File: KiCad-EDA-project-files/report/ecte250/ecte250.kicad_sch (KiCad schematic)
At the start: 8 parts, among them U1 LM2596S-5, U2 ADXL343

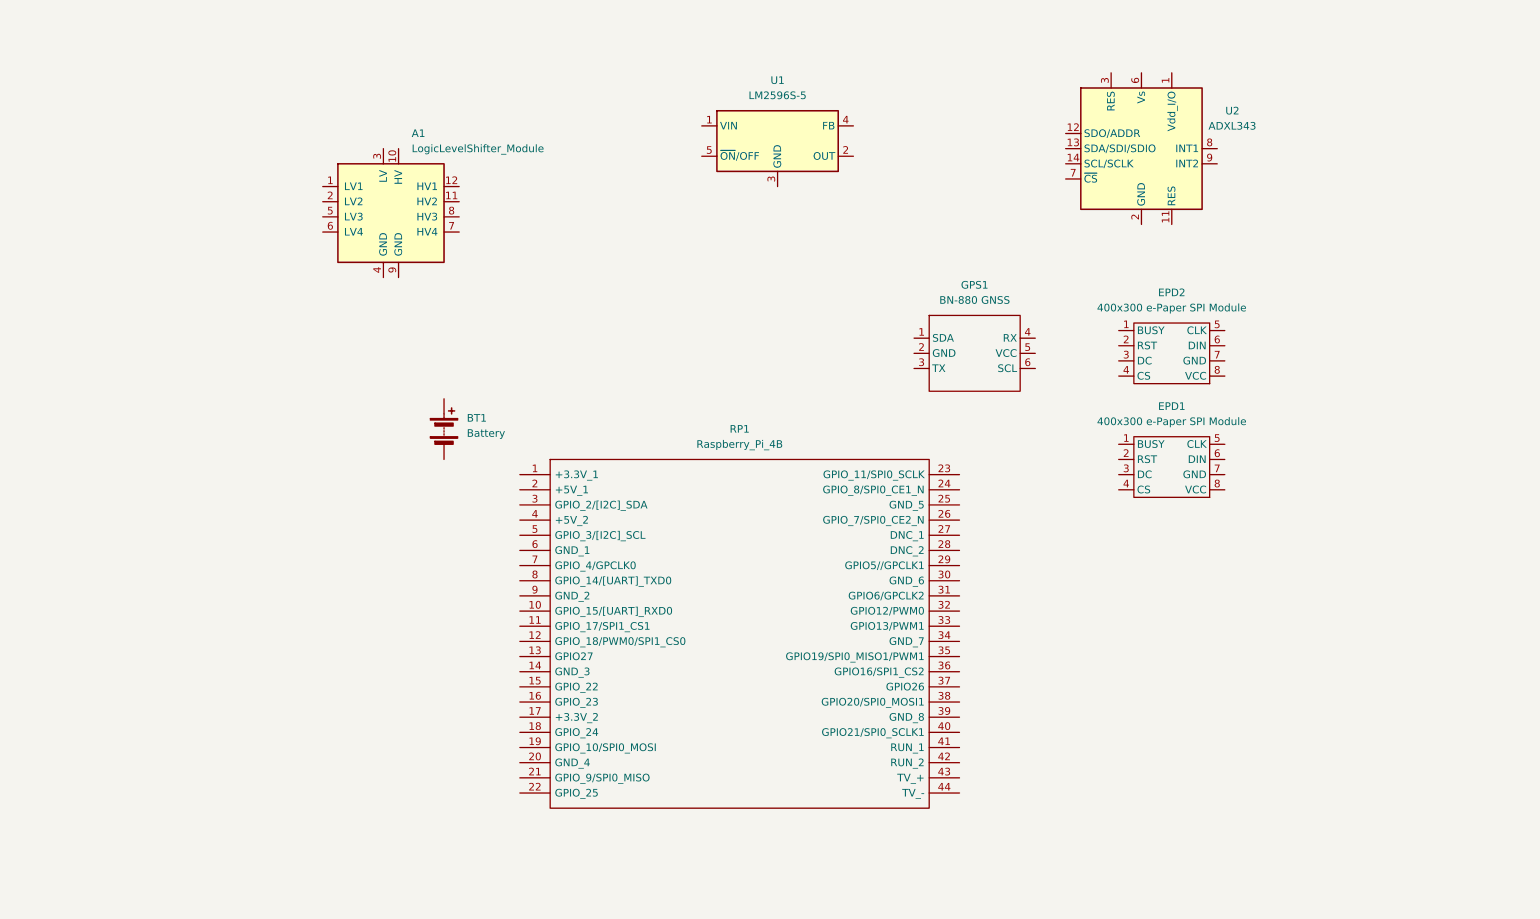
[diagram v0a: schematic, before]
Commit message: Added components used in exhibition
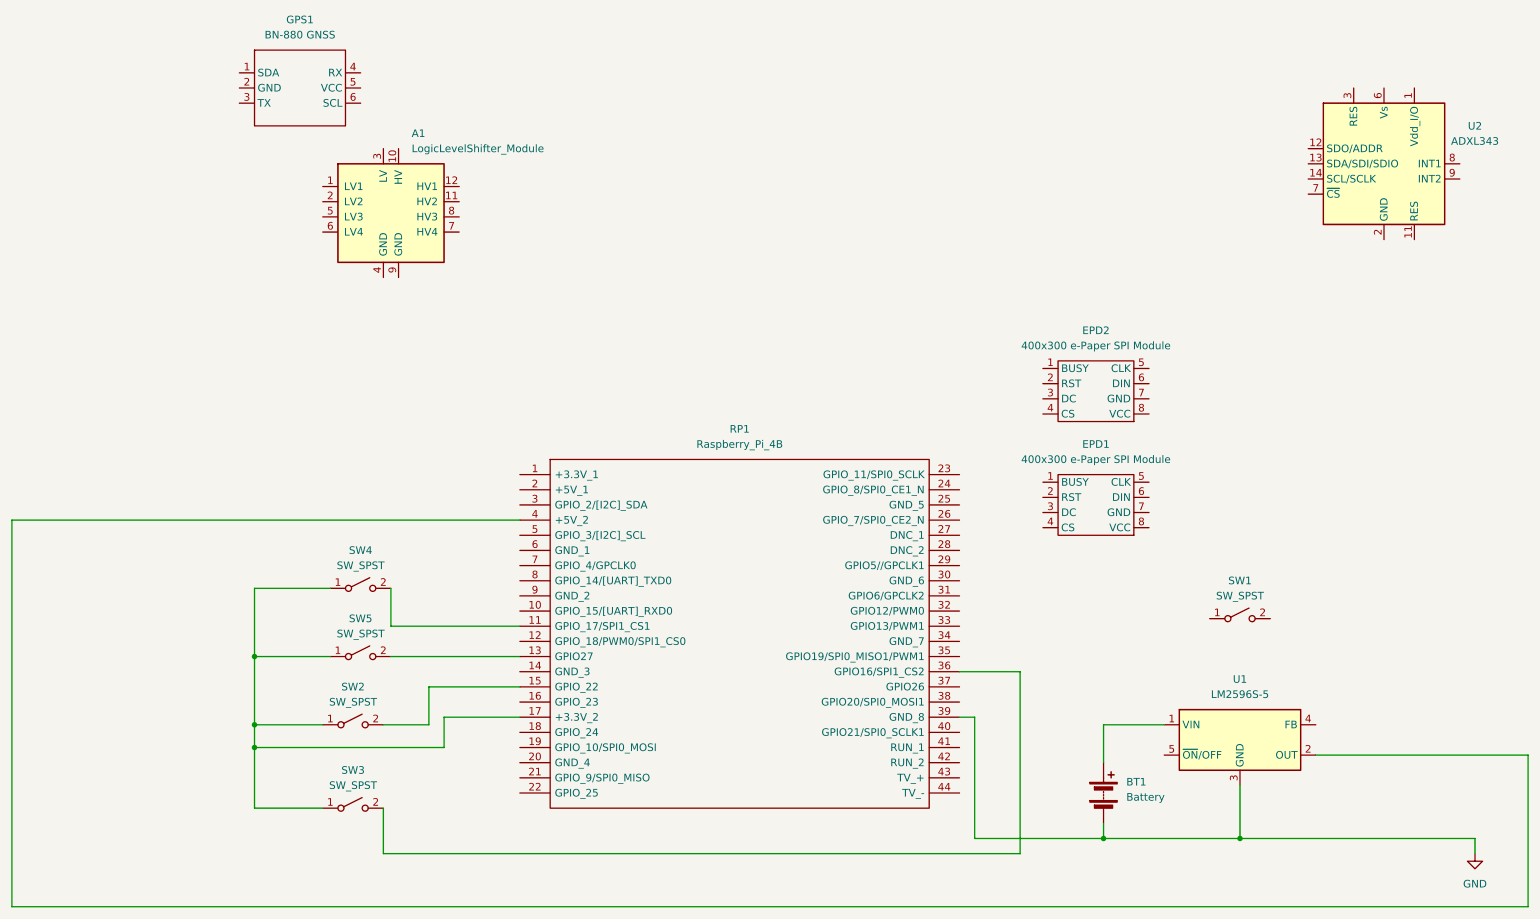
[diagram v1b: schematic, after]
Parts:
- added SW1, SW2, SW3, SW4, SW5: SW_SPST, symbol Switch:SW_SPST
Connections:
- net at U1.1 (VIN): now also BT1.1 (+)
- net at U1.2 (OUT): now also RP1.4 (+5V_2)
- net GND: now reaches U1.3 (GND)
- net GND: now also BT1.2 (-), RP1.39 (GND_8)
- net at RP1.11 (GPIO_17/SPI1_CS1): now also SW4.2 (B)
- net at RP1.13 (GPIO27): now also SW5.2 (B)
- net at RP1.15 (GPIO_22): now also SW2.2 (B)
- net at RP1.17 (+3.3V_2): now also SW2.1 (A), SW3.1 (A), SW4.1 (A), SW5.1 (A)
- net at RP1.36 (GPIO16/SPI1_CS2): now also SW3.2 (B)
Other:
- moved on the sheet: BT1, EPD1, EPD2, GPS1, U1, U2

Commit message: updated schematic files
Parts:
- BT1: value Battery -> 2s Li-Po
- U2: value ADXL343 -> ADXL345
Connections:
- net GND: now also A1.4 (GND), A1.9 (GND), EPD1.7 (GND), EPD2.7 (GND), GPS1.2 (GND), U2.2 (GND), U2.4 (GND), U2.5 (GND)
- net at U1.2 (OUT): now also SW1.1 (A); no longer RP1.4 (+5V_2)
- net at A1.1 (LV1): now also RP1.10 (GPIO_15/[UART]_RXD0)
- net at A1.10 (HV): now also GPS1.5 (VCC), RP1.2 (+5V_1)
- net at A1.11 (HV2): now also GPS1.4 (RX)
- net at A1.12 (HV1): now also GPS1.3 (TX)
- net at A1.2 (LV2): now also RP1.8 (GPIO_14/[UART]_TXD0)
- net at A1.3 (LV): now also EPD1.8 (VCC), EPD2.8 (VCC), RP1.1 (+3.3V_1), U2.6 (Vs)
- net at A1.7 (HV4): now also GPS1.1 (SDA)
- net at A1.8 (HV3): now also GPS1.6 (SCL)
- net at SW1.2 (B): now also RP1.4 (+5V_2)
- net at RP1.23 (GPIO_11/SPI0_SCLK): now also EPD1.5 (CLK), EPD2.5 (CLK)
- net at RP1.3 (GPIO_2/[I2C]_SDA): now also U2.13 (SDA/SDI/SDIO)
- net at RP1.5 (GPIO_3/[I2C]_SCL): now also U2.14 (SCL/SCLK)
- no-connect marks 0 -> 9
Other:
- moved on the sheet: A1, EPD1, GPS1, RP1, SW1

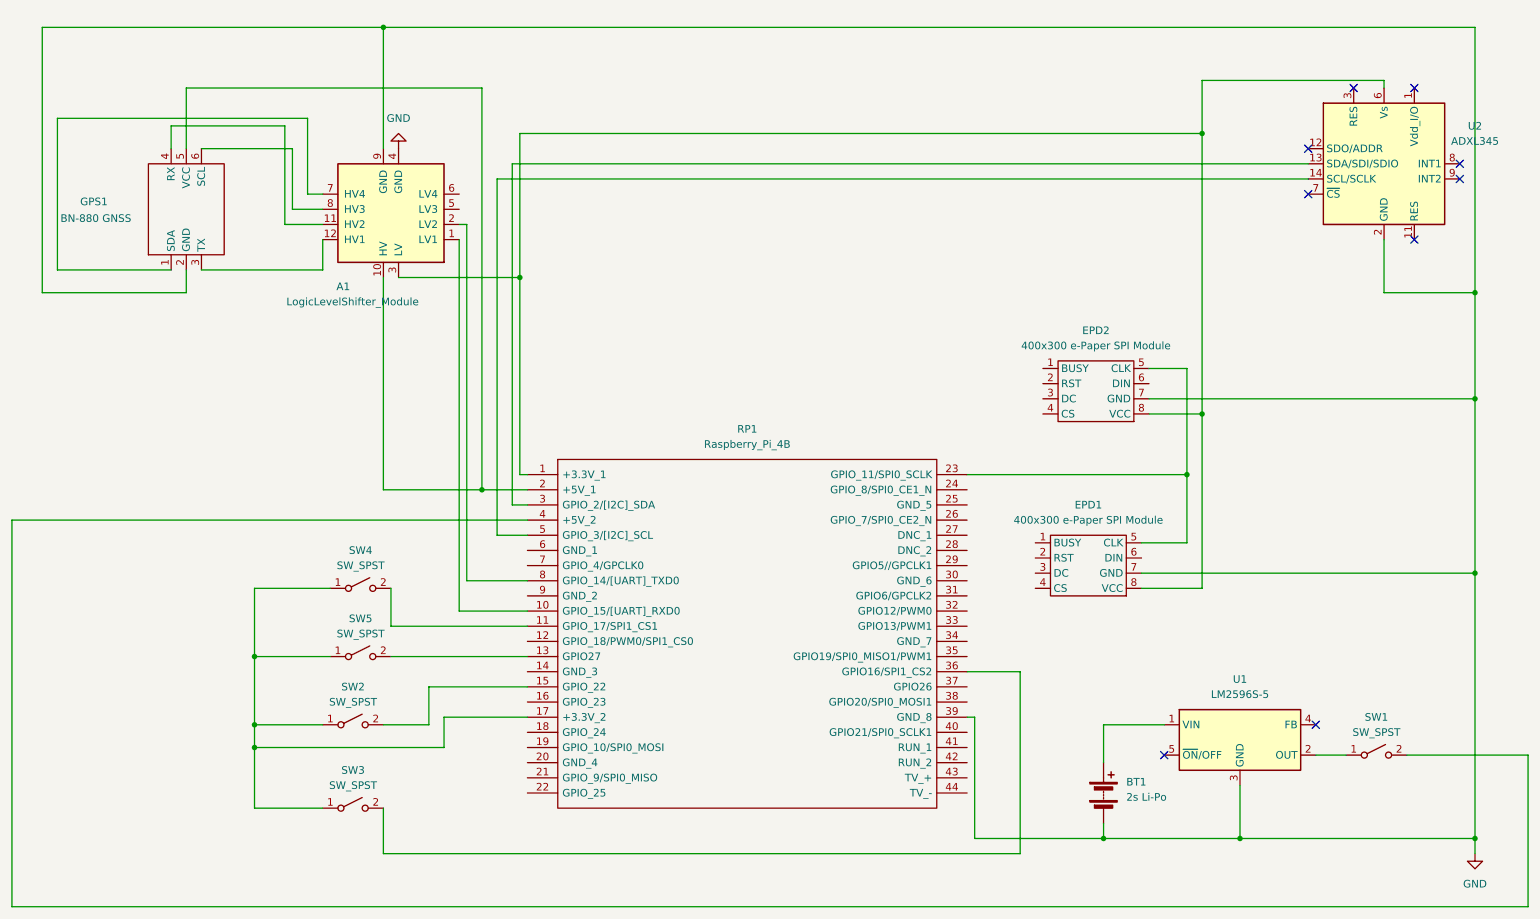
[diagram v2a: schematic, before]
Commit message: updated schematic. changed epd1config pin map
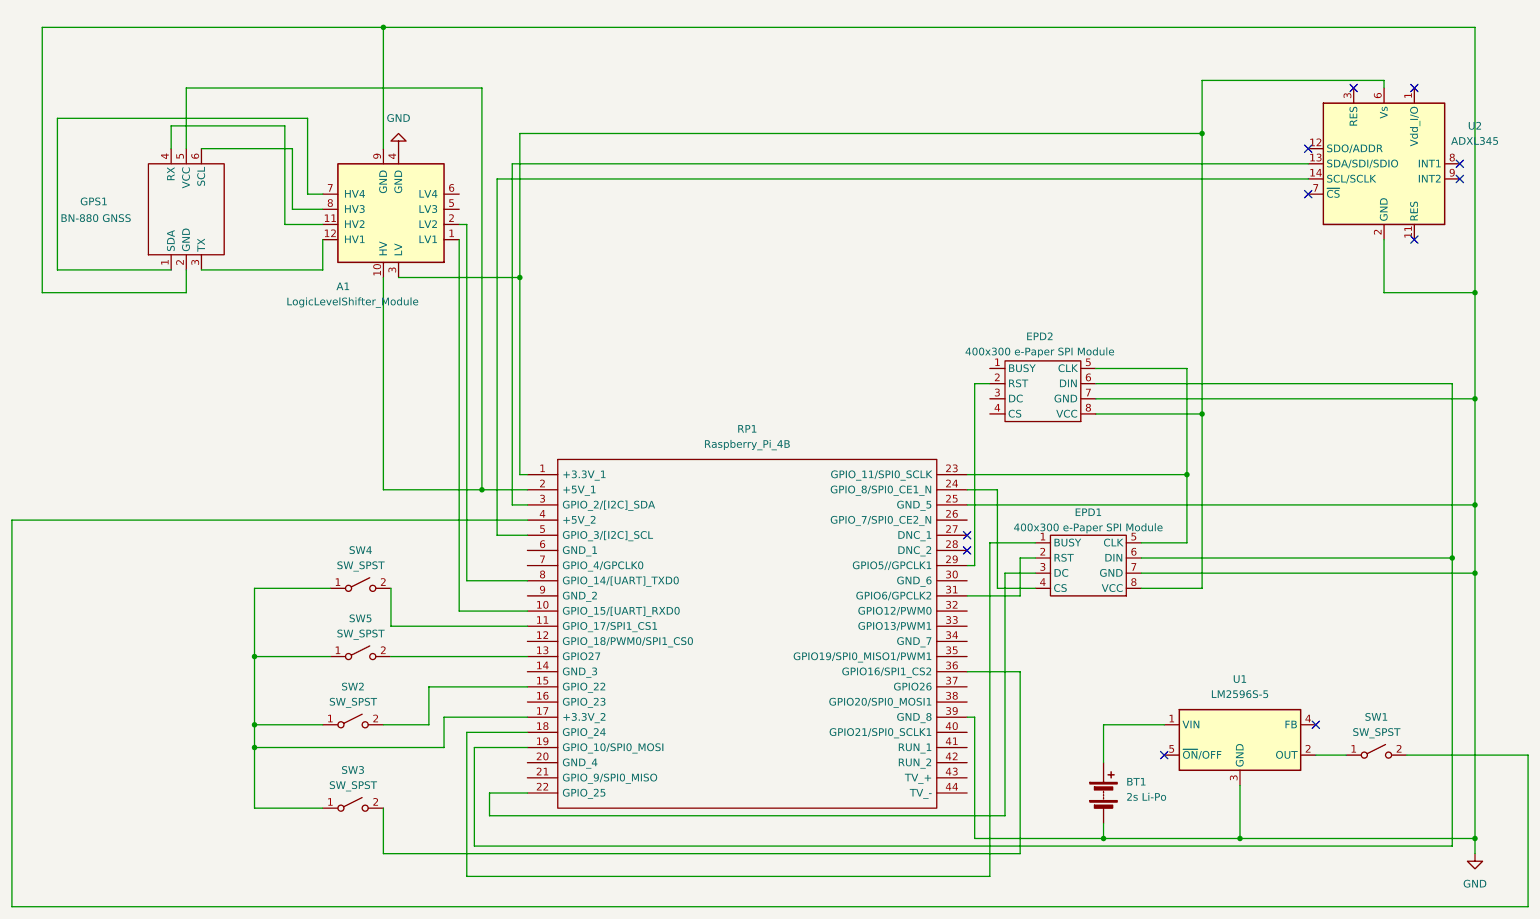
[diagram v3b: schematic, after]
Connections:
- net GND: now also RP1.25 (GND_5)
- net at RP1.18 (GPIO_24): now also EPD1.1 (BUSY)
- net at RP1.19 (GPIO_10/SPI0_MOSI): now also EPD1.6 (DIN), EPD2.6 (DIN)
- net at RP1.22 (GPIO_25): now also EPD1.3 (DC)
- net at RP1.24 (GPIO_8/SPI0_CE1_N): now also EPD1.4 (CS)
- net at RP1.29 (GPIO5//GPCLK1): now also EPD2.2 (RST)
- net at RP1.31 (GPIO6/GPCLK2): now also EPD1.2 (RST)
- no-connect marks 9 -> 11
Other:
- moved on the sheet: EPD2

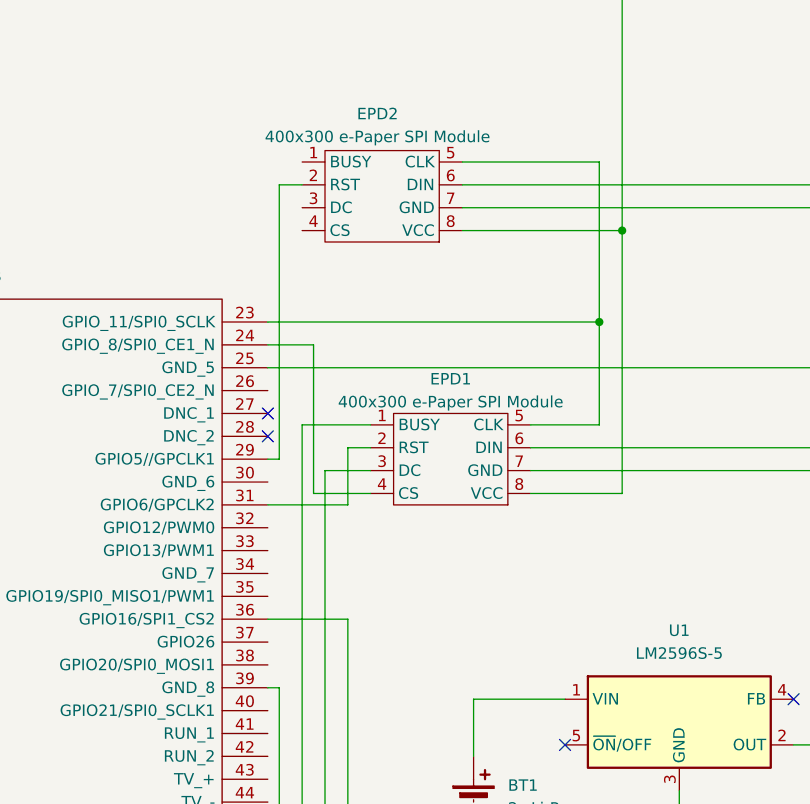
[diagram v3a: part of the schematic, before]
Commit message: updated schematic. Changed epd2config pin map
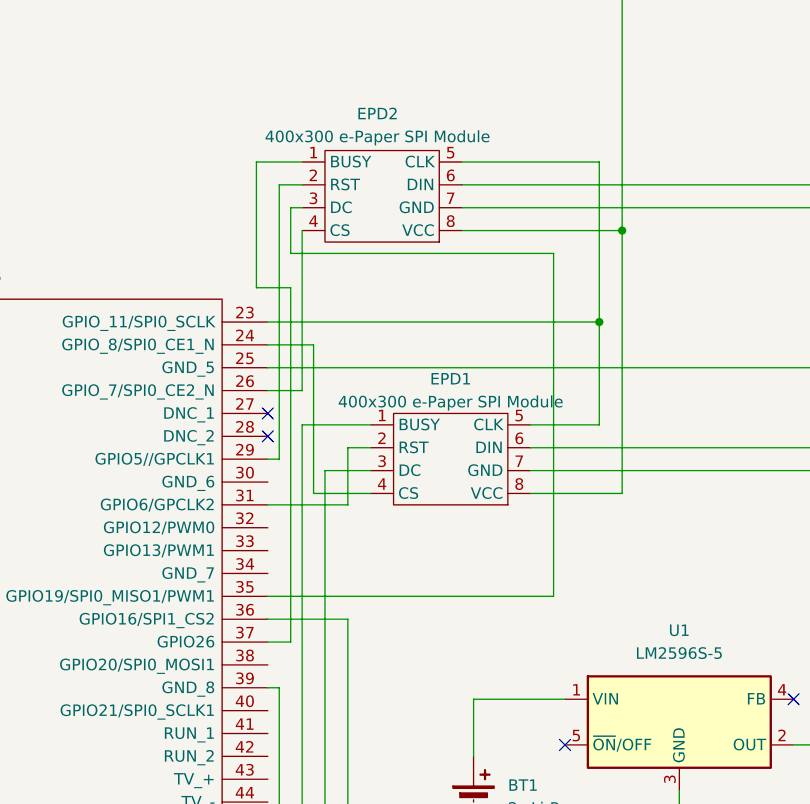
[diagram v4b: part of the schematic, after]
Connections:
- net at RP1.26 (GPIO_7/SPI0_CE2_N): now also EPD2.4 (CS)
- net at RP1.35 (GPIO19/SPI0_MISO1/PWM1): now also EPD2.3 (DC)
- net at RP1.37 (GPIO26): now also EPD2.1 (BUSY)
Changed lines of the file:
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@@
+	(wire
+		(pts
+			(xy 181.61 97.79) (xy 177.8 97.79)
+		)
+		(stroke
+			(width 0)
+			(type default)
+		)
+	)
 	(wire
 		(pts
@@
 	(wire
 		(pts
+			(xy 209.55 82.55) (xy 180.34 82.55)
+		)
+		(stroke
+			(width 0)
+			(type default)
+		)
+	)
+	(wire
+		(pts
 			(xy 271.78 137.16) (xy 271.78 162.56)
 		)
@@
 	(wire
 		(pts
+			(xy 176.53 72.39) (xy 176.53 86.36)
+		)
+		(stroke
+			(width 0)
+			(type default)
+		)
+	)
+	(wire
+		(pts
 			(xy 97.79 147.32) (xy 184.15 147.32)
 		)
@@
 	(wire
 		(pts
+			(xy 180.34 86.36) (xy 180.34 125.73)
+		)
+		(stroke
+			(width 0)
+			(type default)
+		)
+	)
+	(wire
+		(pts
 			(xy 104.14 143.51) (xy 97.79 143.51)
 		)
@@
 	(wire
 		(pts
+			(xy 176.53 86.36) (xy 180.34 86.36)
+		)
+		(stroke
+			(width 0)
+			(type default)
+		)
+	)
+	(wire
+		(pts
 			(xy 17.78 97.79) (xy 104.14 97.79)
 		)
@@
 	(wire
 		(pts
+			(xy 209.55 120.65) (xy 209.55 82.55)
+		)
+		(stroke
+			(width 0)
+			(type default)
+		)
+	)
+	(wire
+		(pts
 			(xy 49.53 55.88) (xy 69.85 55.88)
 		)
@@
 	(wire
 		(pts
+			(xy 180.34 77.47) (xy 181.61 77.47)
+		)
+		(stroke
+			(width 0)
+			(type default)
+		)
+	)
+	(wire
+		(pts
 			(xy 262.89 59.69) (xy 262.89 15.24)
 		)
@@
 	(wire
 		(pts
+			(xy 180.34 82.55) (xy 180.34 77.47)
+		)
+		(stroke
+			(width 0)
+			(type default)
+		)
+	)
+	(wire
+		(pts
 			(xy 80.01 153.67) (xy 186.69 153.67)
 		)
@@
 	(wire
 		(pts
+			(xy 177.8 120.65) (xy 209.55 120.65)
+		)
+		(stroke
+			(width 0)
+			(type default)
+		)
+	)
+	(wire
+		(pts
 			(xy 259.08 104.14) (xy 259.08 74.93)
 		)
@@
 	(wire
 		(pts
+			(xy 181.61 72.39) (xy 176.53 72.39)
+		)
+		(stroke
+			(width 0)
+			(type default)
+		)
+	)
+	(wire
+		(pts
 			(xy 179.07 151.13) (xy 200.66 151.13)
 		)
@@
 	(wire
 		(pts
+			(xy 180.34 125.73) (xy 177.8 125.73)
+		)
+		(stroke
+			(width 0)
+			(type default)
+		)
+	)
+	(wire
+		(pts
 			(xy 22.86 59.69) (xy 22.86 15.24)
 		)
@@
 		)
 		(stroke
+			(width 0)
+			(type default)
+		)
+	)
+	(wire
+		(pts
+			(xy 181.61 80.01) (xy 181.61 97.79)
+		)
+		(stroke
